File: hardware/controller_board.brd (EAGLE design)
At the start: 144 x 118 mm, 51 parts, among them J1 FRSKY-GIMBAL, J2 FRSKY-GIMBAL, J3 WIRE-HARNESS-SPARKFUN-9915, J4 AVR_SPI_PRG_6NS, J7 FTDI_BASICPTH, SW1 PUSHBUTTON_SMD-VERTICAL-1, SW2 PUSHBUTTON_SMD-VERTICAL-1, SW3 PUSHBUTTON_SMD-VERTICAL-1, SW4 PUSHBUTTON_SMD-VERTICAL-1, SW5 PUSHBUTTON_SMD-VERTICAL-1, U1 ATMEGA128RFA1, U2 TPS73633-DBVT3.3V, Y1 CRYSTAL5X3

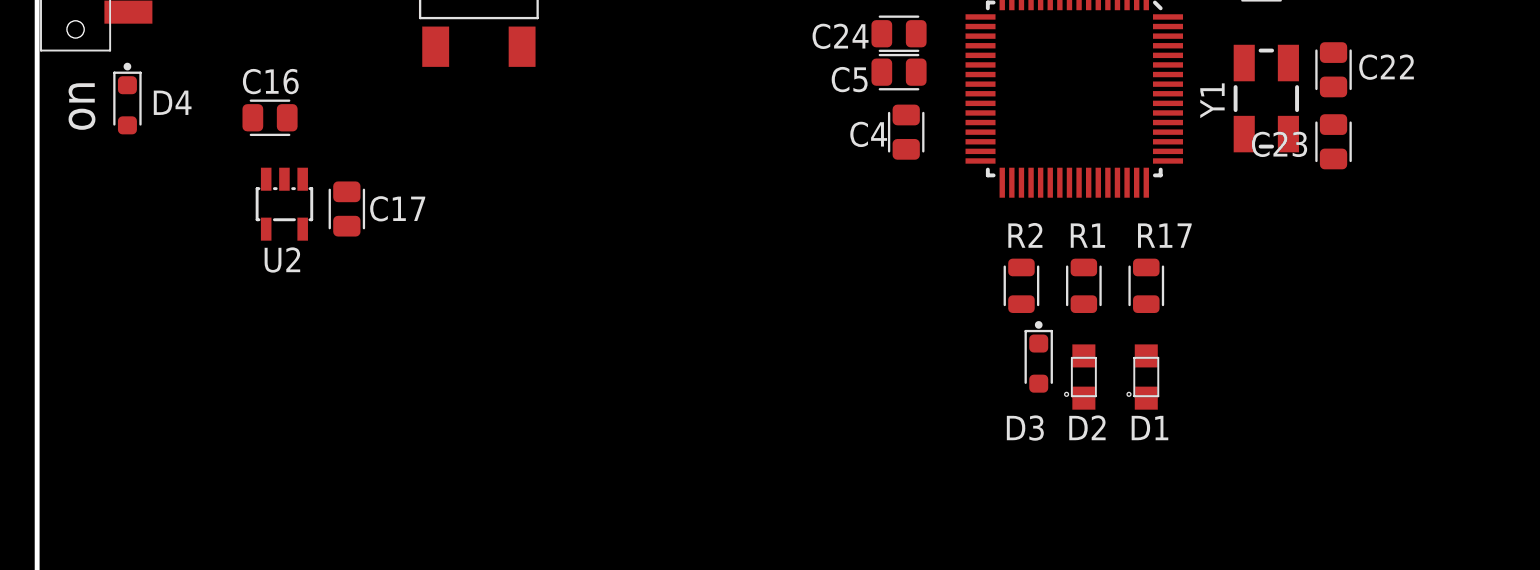
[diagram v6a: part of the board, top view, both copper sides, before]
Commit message: smash and reorg most stuff.  Add 10uF caps
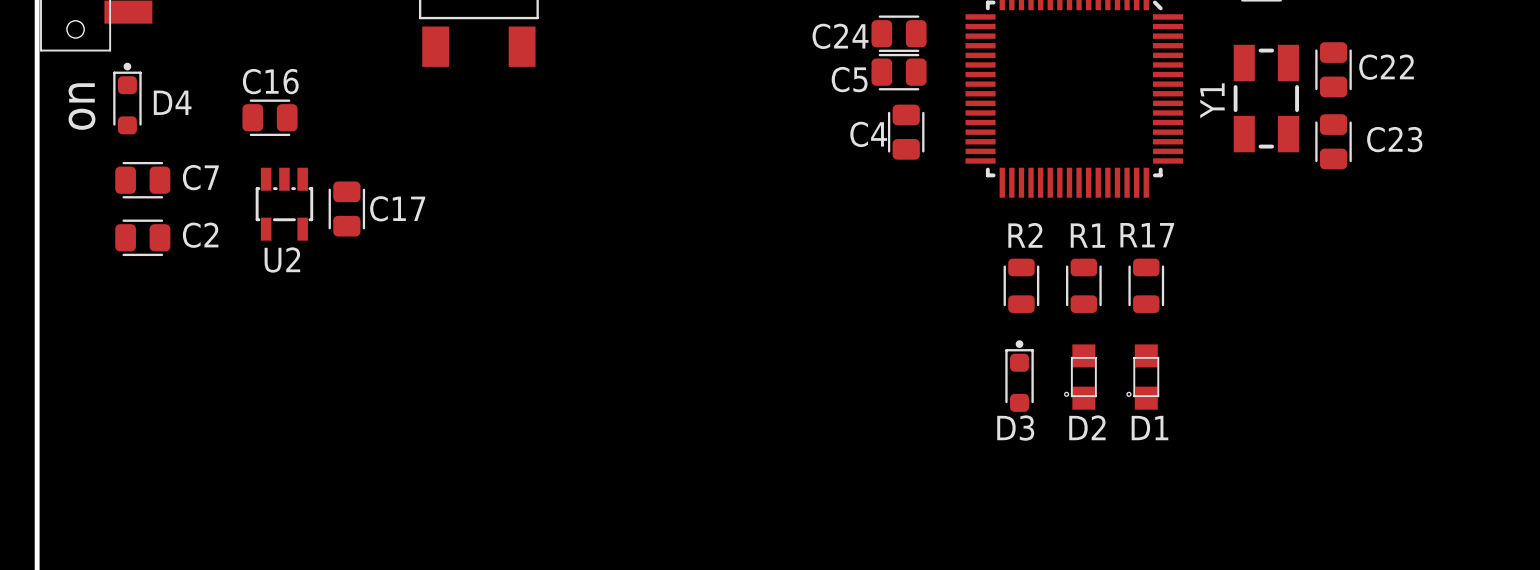
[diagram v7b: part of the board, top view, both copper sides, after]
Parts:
- added C2, C7: 10uF, quadparts_prebuilt:CAPC2012X140_HS
- moved D3 1.41 mm to (-21.8, 21.2)
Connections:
- new net 3.3V: J4.2, J7.VCC
- net +3V3: now also C7.1
- net GND: now also C2.2, C7.2
- net VBAT: now also C2.1

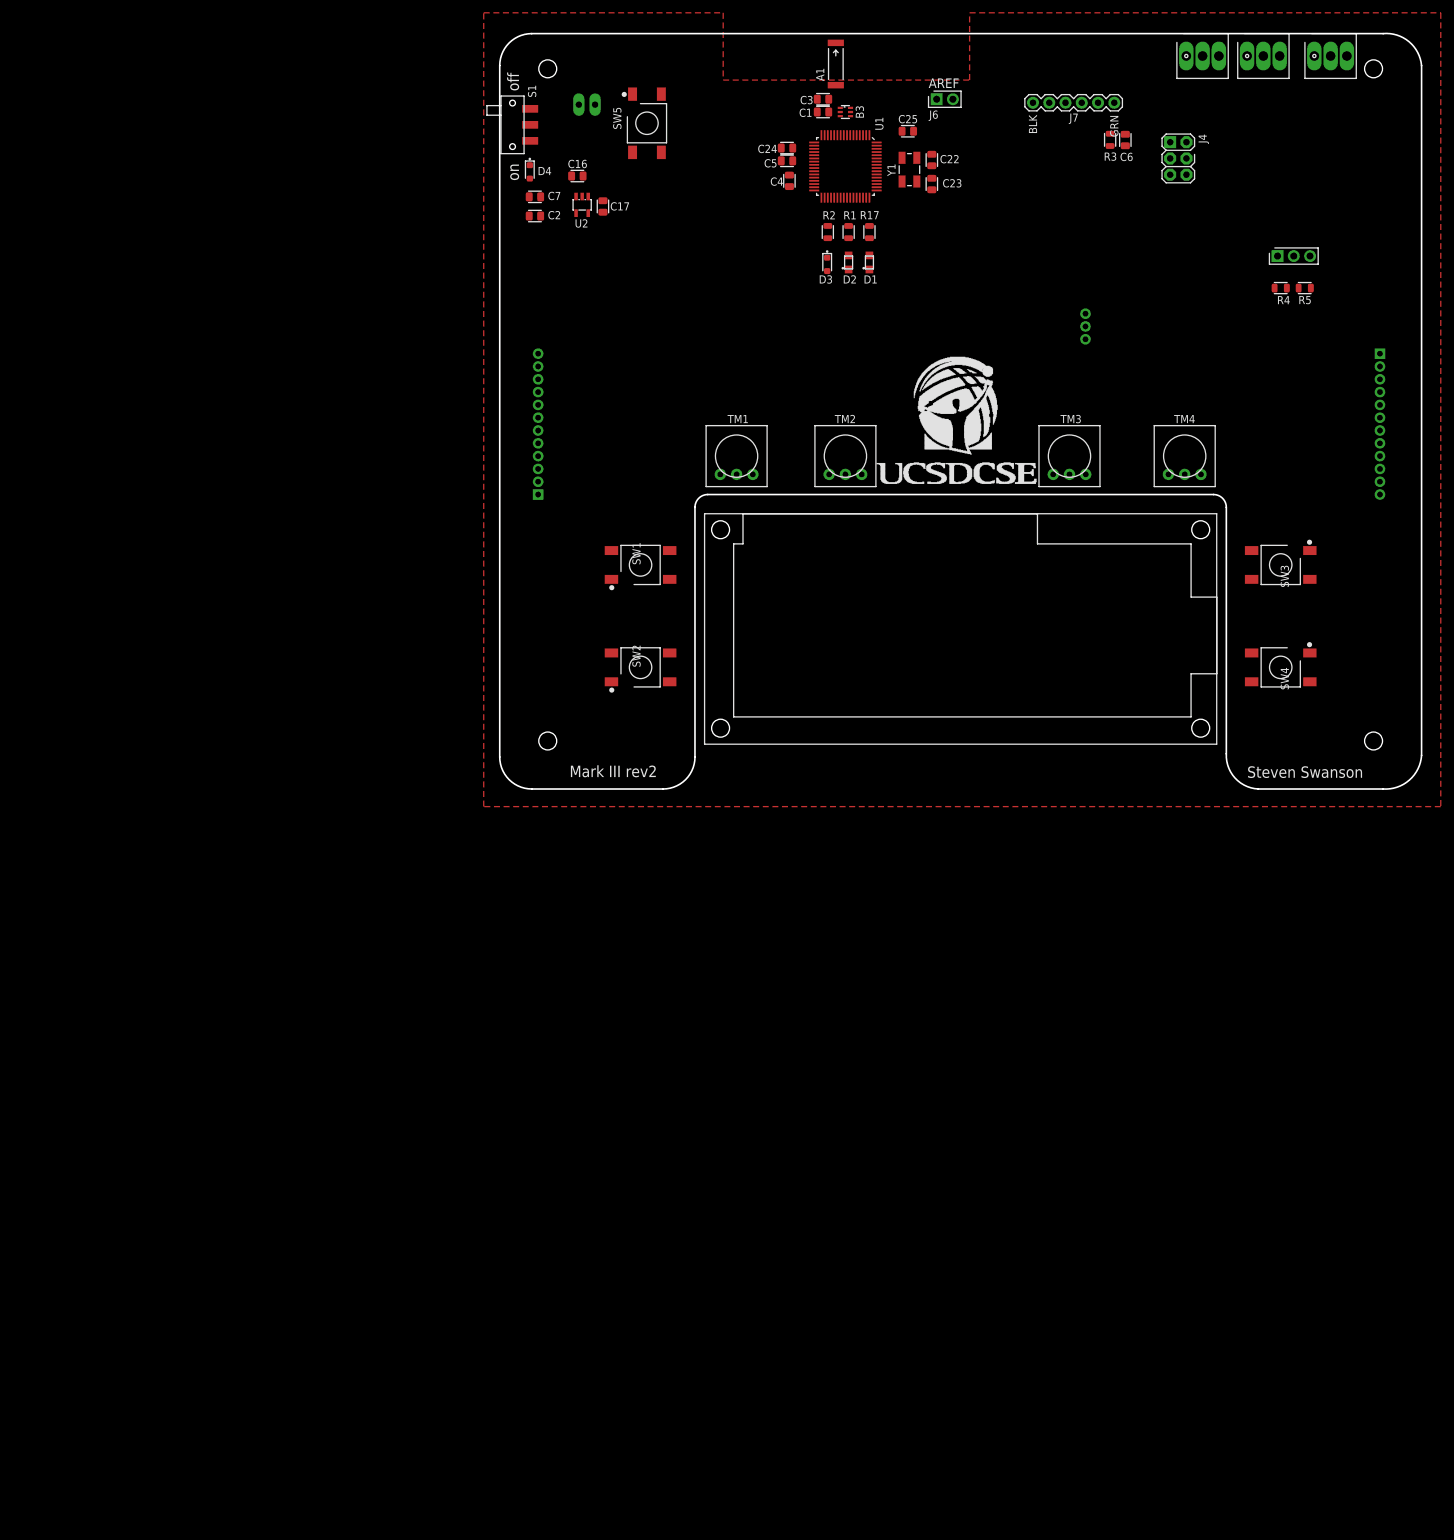
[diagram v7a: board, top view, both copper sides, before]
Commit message: first draft of FTDI integration
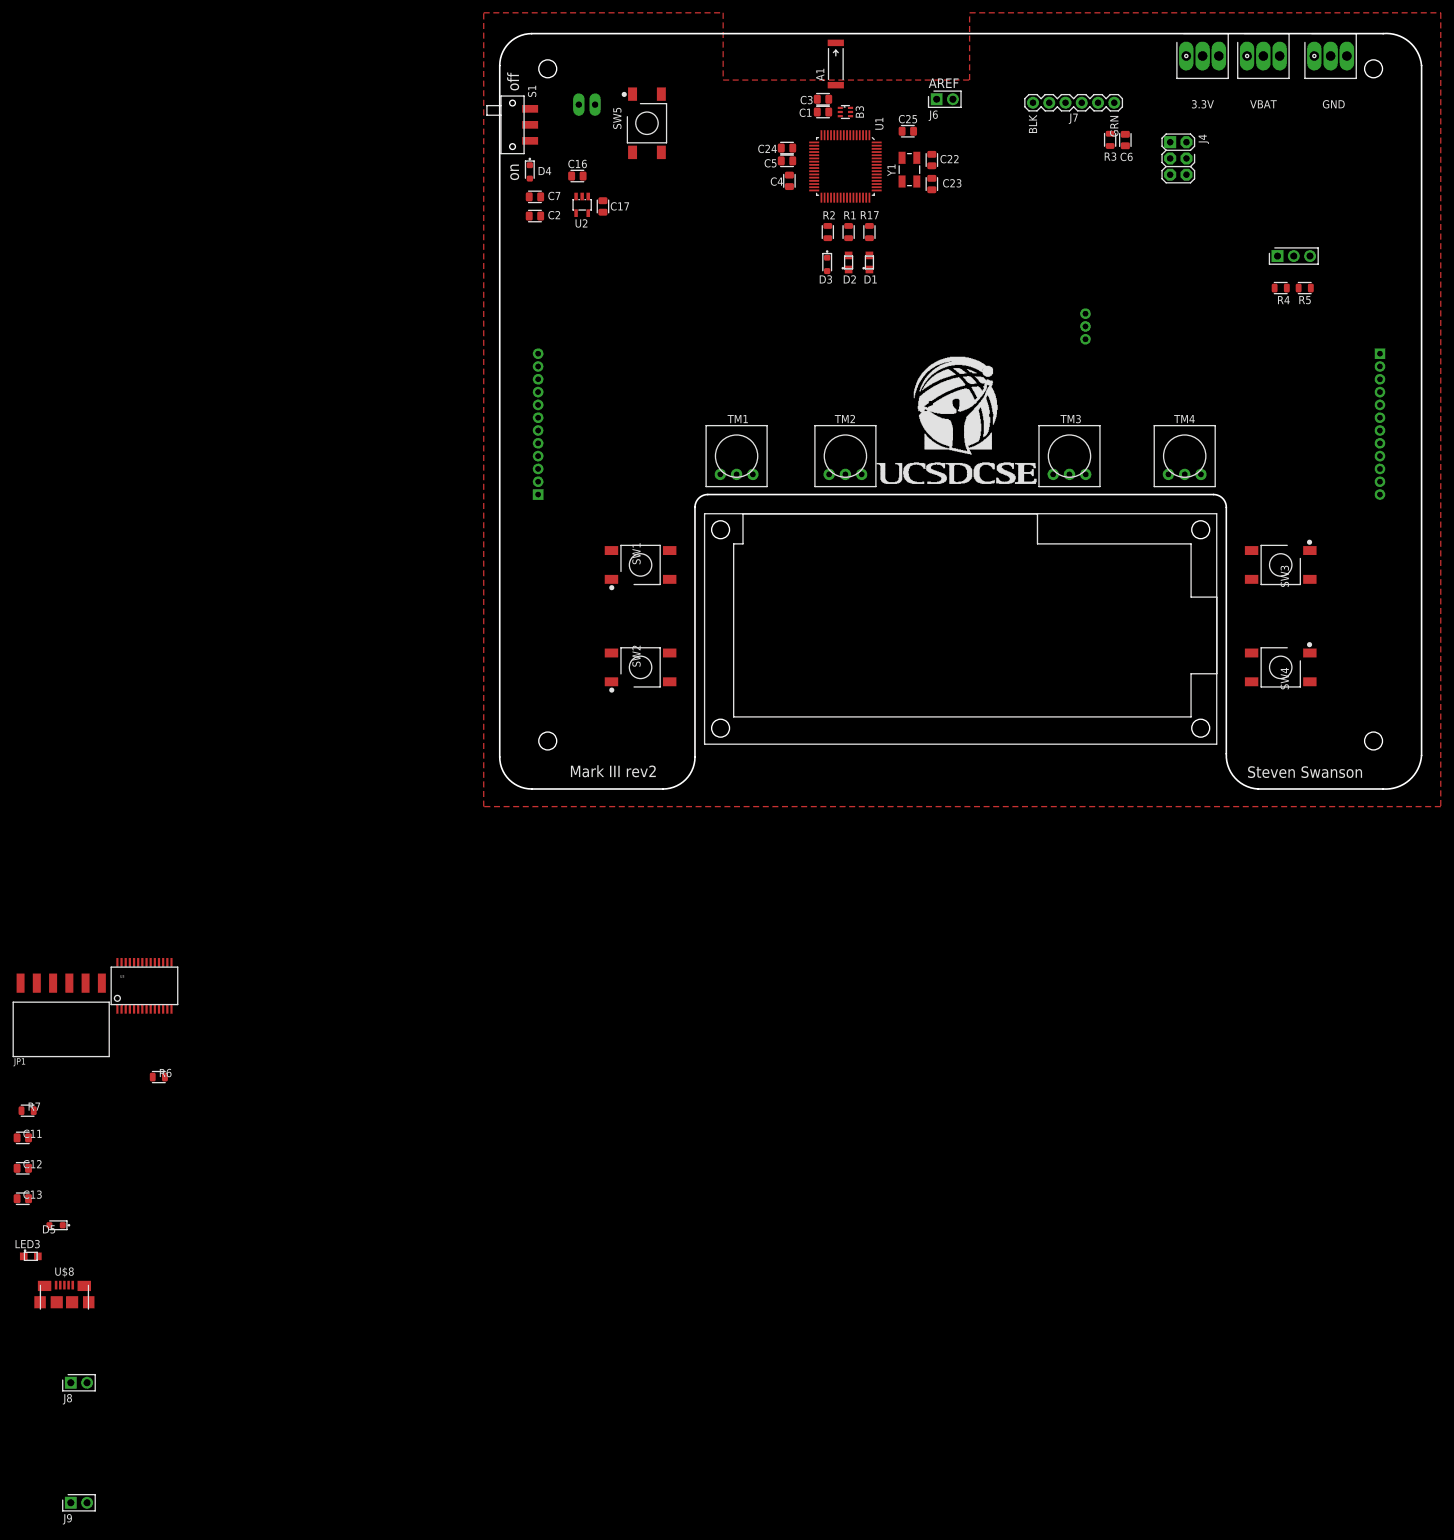
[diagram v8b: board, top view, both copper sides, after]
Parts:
- added C11, C13: 0.1uF, quadparts_prebuilt:CAPC2012X140_HS
- added C12: 10uF, quadparts_prebuilt:CAPC2012X140_HS
- added D5: green, quadparts_prebuilt:LEDSC125X200X120-2_HS
- added J8, J9: (no value), custom:MALE_HEADER_2X1_0.1IN
- added JP1: (no value), SparkFun:1X06-SMD-FEMALE-V2
- added LED3: LED-RED, custom:LED_LTST-C170EKT
- added R6, R7: 1K, quadparts_prebuilt:RESC2012X60_HS
- added U$8: USB-MICROA-AMPHENOL-10118192-0001LF, RemoteParts:USB-MICROA-10118192-0001LF
- added U3: FT232RLSSOP, SparkFun:SSOP28DB
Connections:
- removed net N$11: C6.2, J7.DTR
- removed net RX0: J7.TXO, U1.46
- removed net TX0: J7.RXI, U1.47
- new net 5V: C11.1, C12.1, R6.2, R7.2, U$8.1, U3.20
- new net CTS: J7.CTS, JP1.2, U3.11
- new net DTR: C6.2, J7.DTR, JP1.6, U3.2
- new net FTDI+3V3: C13.1, J8.1, JP1.3, U3.17, U3.4
- new net N$2: LED3.A, R6.1
- new net N$3: D5.A, R7.1
- new net REG+3V3: J9.1, U2.5
- new net RXI: J7.RXI, JP1.5, U1.47, U3.5
- new net RXLED: D5.C, U3.22
- new net TXLED: LED3.C, U3.23
- new net TXO: J7.TXO, JP1.4, U1.46, U3.1
- new net USB_D+: U$8.3, U3.15
- new net USB_D-: U$8.2, U3.16
- net +3V3: now also J7.VCC, J8.2, J9.2; no longer U2.5
- net 3.3V: no longer J7.VCC
- net GND: now also C11.2, C12.2, C13.2, JP1.1, U$8.10, U$8.11, U$8.5, U$8.6, U$8.7, U$8.8, U$8.9, U3.18, U3.21, U3.25, U3.26, U3.7
